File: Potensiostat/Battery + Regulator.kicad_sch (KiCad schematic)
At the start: 13 parts, among them J2 Conn_01x02_Pin, Q2 Q_PMOS, U3 TP4057, U4 TCR3DF335_LMCT

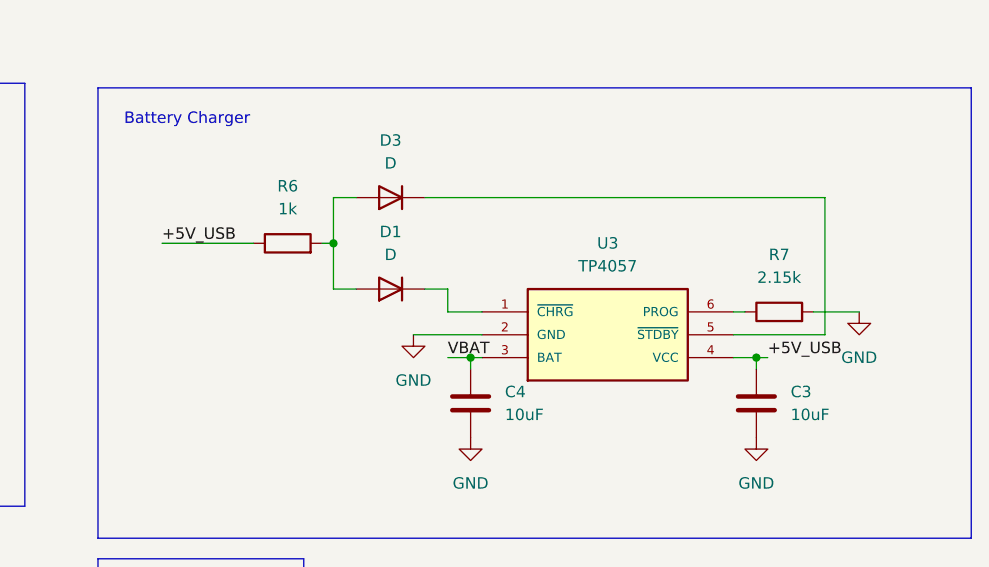
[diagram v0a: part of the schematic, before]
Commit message: Added LMP USP-UART
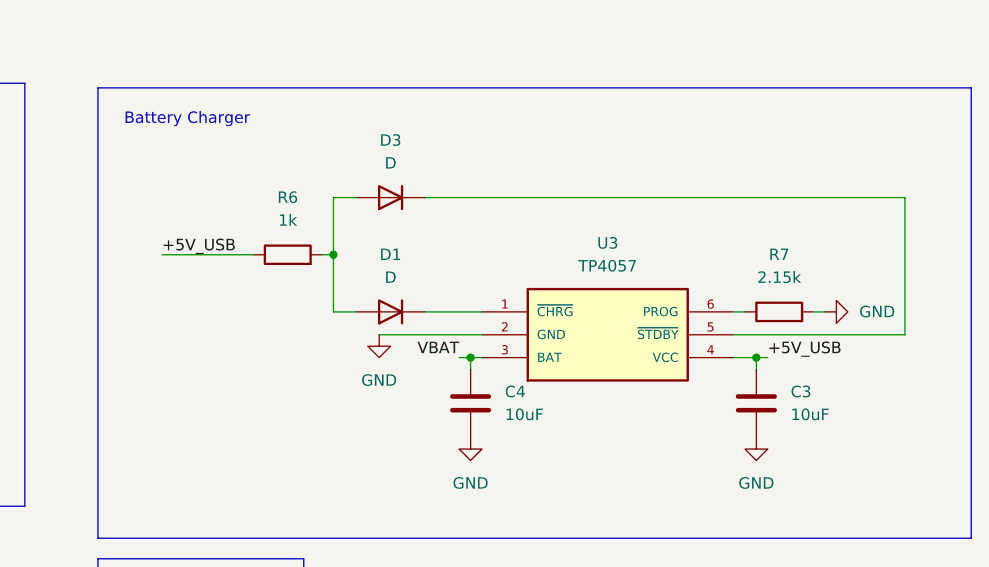
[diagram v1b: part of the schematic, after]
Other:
- moved on the sheet: D1, R6
